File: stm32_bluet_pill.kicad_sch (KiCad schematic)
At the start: 0 parts

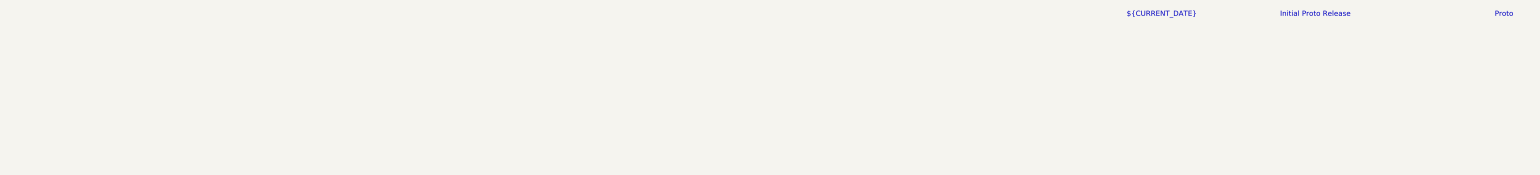
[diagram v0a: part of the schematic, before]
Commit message: Updated project
- Changed board stackup, trace-widths
- Changed VIA size
- Fixed fab drawings
- added CHG FLT LED
- Removed unnecessary files
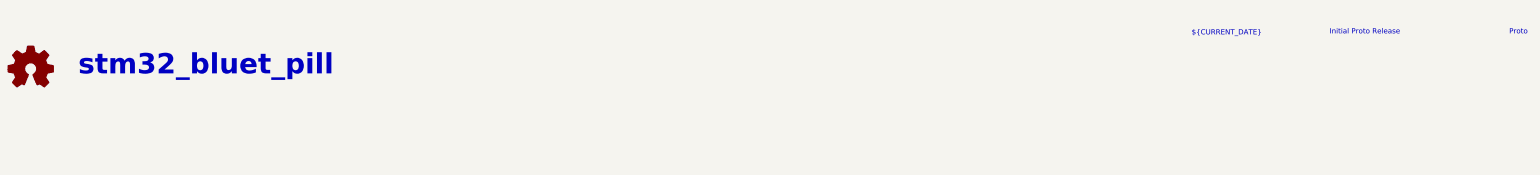
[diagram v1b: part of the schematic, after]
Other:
- note added: "${TITLE}"
- company: Clover Designs -> Brendan Bleker
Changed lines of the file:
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@@
 	(title_block
 		(title "stm32_bluet_pill")
-		(date "2024-04-03")
+		(date "2024-04-17")
 		(rev "Proto")
-		(company "Clover Designs")
-		(comment 1 "Brendan Bleker")
+		(company "Brendan Bleker")
+		(comment 1 "Designed by:")
 	)
 	(text "Proto"
 		(exclude_from_sim no)
-		(at 389.636 18.288 0)
+		(at 393.192 22.606 0)
 		(effects
 			(font
@@
 	(text "${CURRENT_DATE}"
 		(exclude_from_sim no)
-		(at 305.308 18.288 0)
+		(at 321.31 22.86 0)
 		(effects
 			(font
@@
 		)
 	)
+	(text "${TITLE}"
+		(exclude_from_sim no)
+		(at 69.85 30.734 0)
+		(effects
+			(font
+				(size 5 5)
+				(thickness 1)
+				(bold yes)
+			)
+		)
+	)
 	(text "Initial Proto Release"
 		(exclude_from_sim no)
-		(at 343.154 18.288 0)
+		(at 355.346 22.606 0)
 		(effects
 			(font
 				(size 1.27 1.27)
+			)
+		)
+	)
+	(symbol
+		(lib_id "Graphic:Logo_Open_Hardware_Small")
+		(at 26.67 31.75 0)
+		(unit 1)
+		(exclude_from_sim yes)
+		(in_bom no)
+		(on_board no)
+		(dnp no)
+		(fields_autoplaced yes)
+		(property "Reference" "#SYM1"
+			(at 26.67 24.765 0)
+			(effects
+				(font
+					(size 1.27 1.27)
+				)
+				(hide yes)
+			)
+		)
+		(property "Value" "Logo_Open_Hardware_Small"
+			(at 26.67 37.465 0)
+			(effects
+				(font
+					(size 1.27 1.27)
+				)
+				(hide yes)
+			)
+		)
+		(property "Footprint" "Symbol:OSHW-Symbol_6.7x6mm_SilkScreen"
+			(at 26.67 31.75 0)
+			(effects
+				(font
+					(size 1.27 1.27)
+				)
+				(hide yes)
+			)
+		)
+		(property "Datasheet" "~"
+			(at 26.67 31.75 0)
+			(effects
+				(font
+					(size 1.27 1.27)
+				)
+				(hide yes)
+			)
+		)
+		(property "Description" "Open Hardware logo, small"
+			(at 26.67 31.75 0)
+			(effects
+				(font
+					(size 1.27 1.27)
+				)
+				(hide yes)
+			)
+		)
+		(instances
+			(project "stm32_bluet_pill"
+				(path "/45b78866-6047-4631-b3ef-230df13ace1e"
+					(reference "#SYM1")
+					(unit 1)
+				)
 			)
 		)
@@
 		)
 		(instances
-			(project "Bluetooth_OSHW"
-				(path "/45b78866-6047-4631-b3ef-230df13ace1e"
-					(page "4")
+			(project "stm32_bluet_pill"
+				(path "/45b78866-6047-4631-b3ef-230df13ace1e"
+					(page "3")
 				)
 			)
@@
 		)
 		(instances
-			(project "Bluetooth_OSHW"
+			(project "stm32_bluet_pill"
 				(path "/45b78866-6047-4631-b3ef-230df13ace1e"
 					(page "2")
@@
 		)
 		(instances
-			(project "Bluetooth_OSHW"
-				(path "/45b78866-6047-4631-b3ef-230df13ace1e"
-					(page "5")
-				)
-			)
+			(project "stm32_bluet_pill"
+				(path "/45b78866-6047-4631-b3ef-230df13ace1e"
+					(page "4")
+				)
+			)

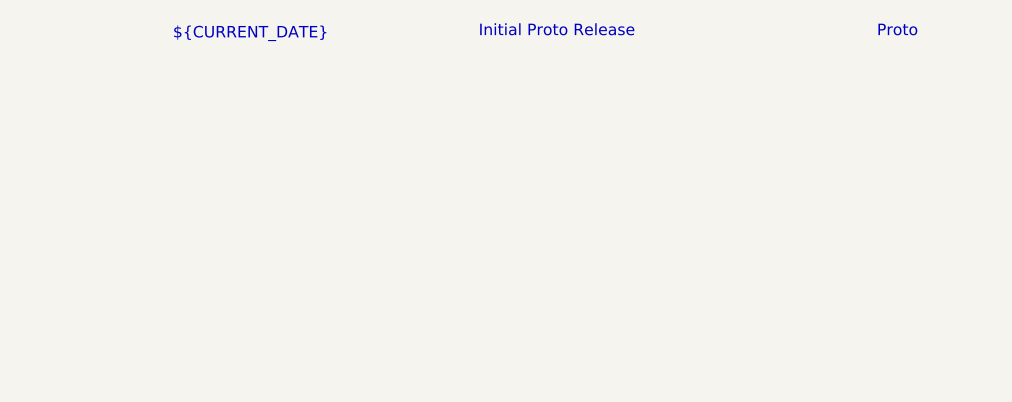
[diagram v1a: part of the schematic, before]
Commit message: Various BOM and Bug Fixes * Changed Stackup to common JLCPCB stackup * Modified trace widths as per new stackup * Reduced drill hole size * Rotated uFL connector as per datasheet pinout * Added pop options for ADC voltage * removed some GPIO and added GND to headers * BOM changes for battery charger, USB connector etc. to support component specifications and USB standards. * Improved MCU bypass and power delivery routing * Various other small bug fixes
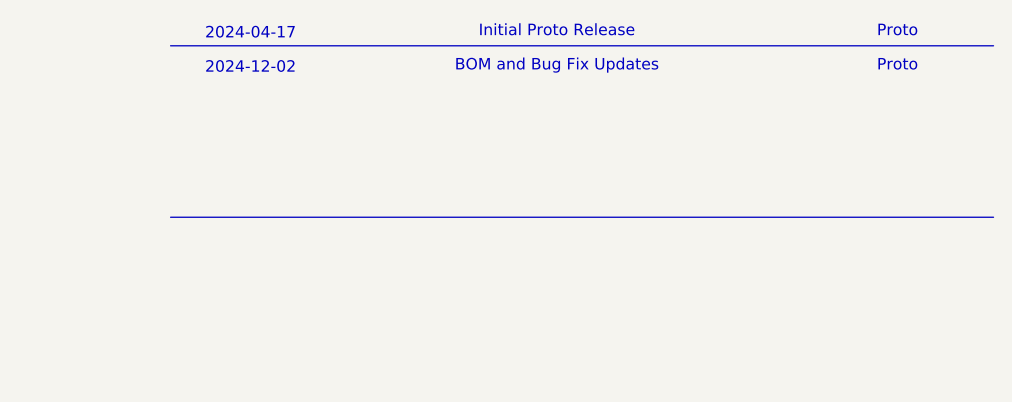
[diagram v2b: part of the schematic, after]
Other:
- note added: "2024-04-17"
- note added: "2024-12-02"
- note added: "BOM and Bug Fix Updates"
- note removed: "${CURRENT_DATE}"
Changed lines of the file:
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@@
 		(title "stm32_bluet_pill")
 		(date "2024-04-17")
-		(rev "Proto")
+		(rev "Proto V2")
 		(company "Brendan Bleker")
 		(comment 1 "Designed by:")
+	)
+	(polyline
+		(pts
+			(xy 312.42 43.18) (xy 403.86 43.18)
+		)
+		(stroke
+			(width 0)
+			(type default)
+			(color 255 255 255 1)
+		)
+	)
+	(polyline
+		(pts
+			(xy 312.42 24.13) (xy 403.86 24.13)
+		)
+		(stroke
+			(width 0)
+			(type default)
+			(color 255 255 255 1)
+		)
 	)
 	(text "Proto"
@@
 		)
 	)
-	(text "${CURRENT_DATE}"
+	(text "2024-04-17"
 		(exclude_from_sim no)
 		(at 321.31 22.86 0)
@@
 		(effects
 			(font
+				(size 1.27 1.27)
+			)
+		)
+	)
+	(text "Proto"
+		(exclude_from_sim no)
+		(at 393.192 26.416 0)
+		(effects
+			(font
+				(size 1.27 1.27)
+			)
+		)
+	)
+	(text "BOM and Bug Fix Updates"
+		(exclude_from_sim no)
+		(at 355.346 26.416 0)
+		(effects
+			(font
+				(size 1.27 1.27)
+			)
+		)
+	)
+	(text "2024-12-02"
+		(exclude_from_sim no)
+		(at 321.31 26.67 0)
+		(effects
+			(font
